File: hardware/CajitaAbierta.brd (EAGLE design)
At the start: 32.1 x 61.8 mm, 30 parts

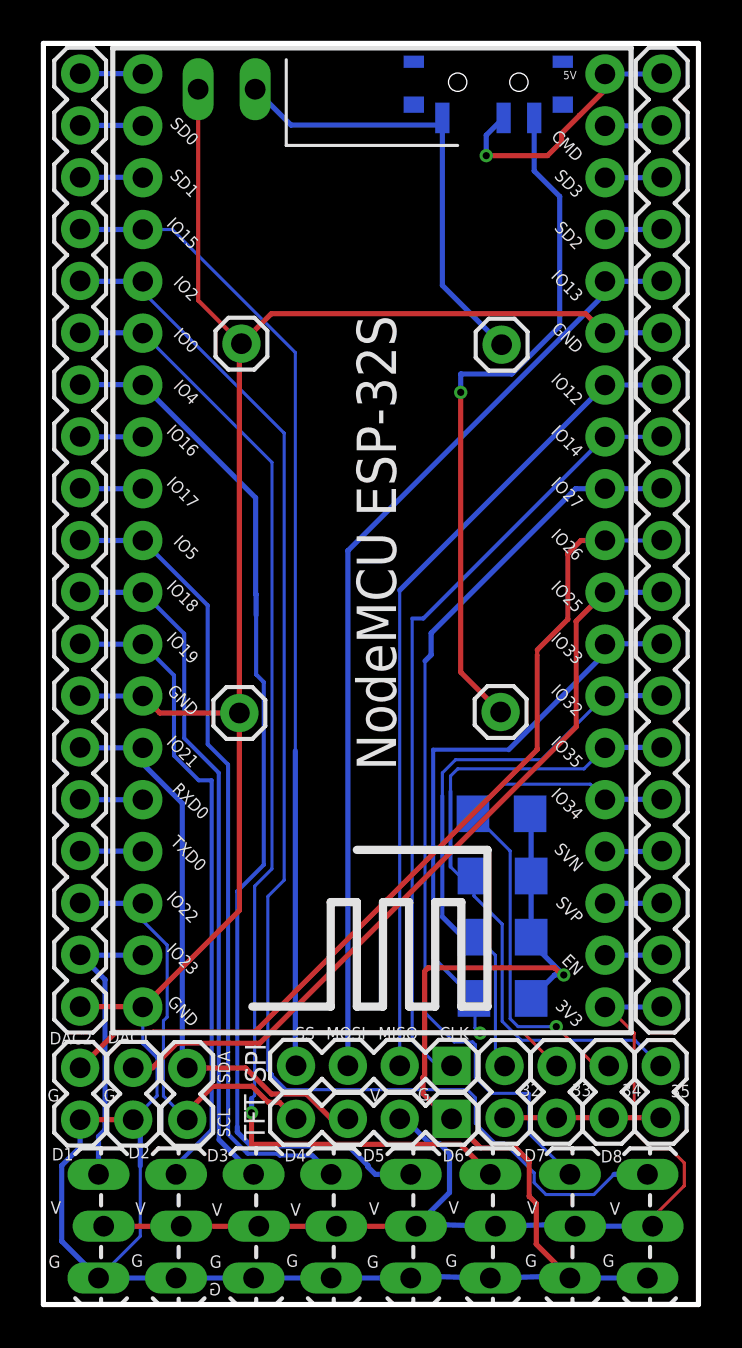
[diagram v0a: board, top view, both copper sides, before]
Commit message: v04 - changes to the TFT connections
nouvelles étiquettes (labels)
cambié sdl and sda
switch on the other side
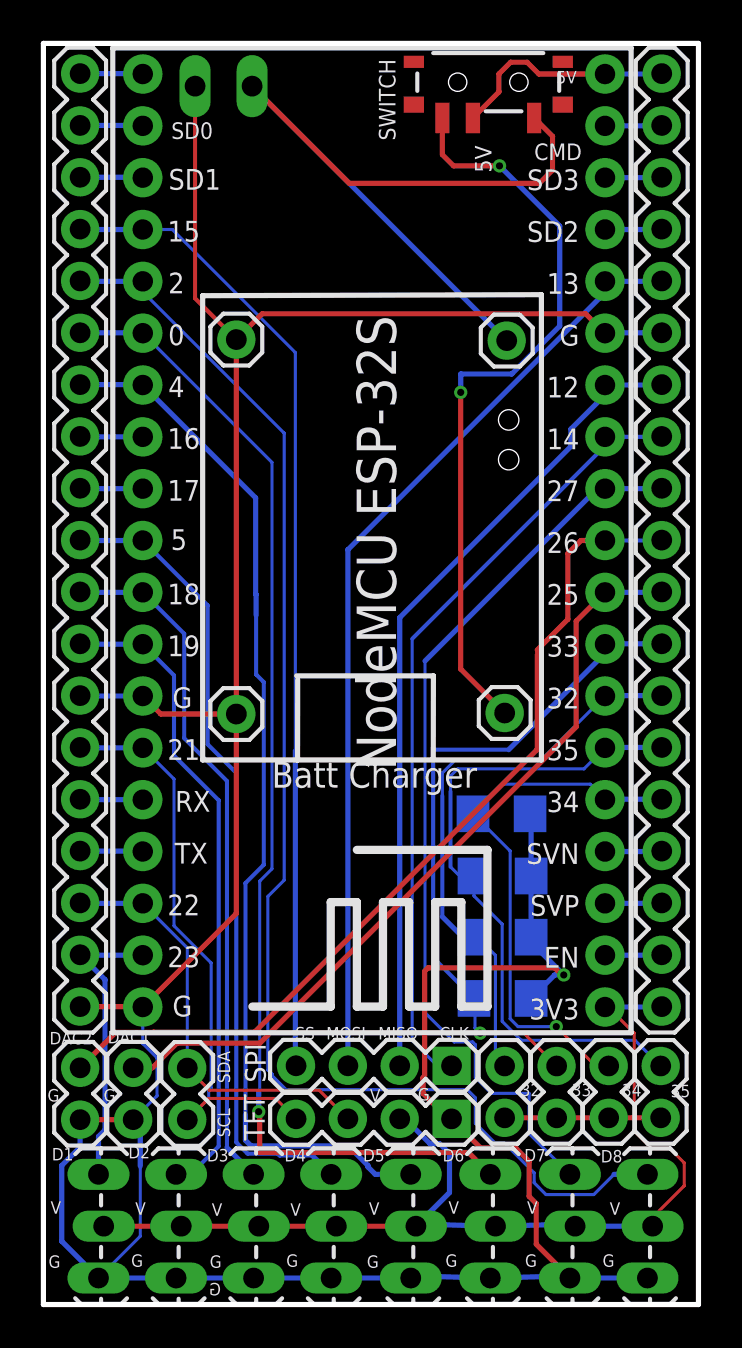
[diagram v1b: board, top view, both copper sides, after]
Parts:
- moved GND 0.32 mm to (9.45, 47.3)
- moved BATT+ 0.32 mm to (22.7, 47.2)
- moved BATT 0.21 mm to (7.56, 59.7)
- moved 5V_IN 0.21 mm to (22.6, 29.0)
- moved BAT- 0.16 mm to (9.45, 28.9)
- flipped SWITCH to the top
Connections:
- net I2C_SCL: now also I2C.2, TFT.3; no longer I2C.1, TFT.4
- net I2C_SDA: now also I2C.1, TFT.4; no longer I2C.2, TFT.3
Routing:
- net BATT+: track 22.6 -> 37.5 mm
- net 5V_IN: track 33.9 -> 37.2 mm, vias 1 -> 2
- net 5V: track 13.2 -> 11.1 mm, vias 1 -> 0
- net I2C_SDA: track 28.6 -> 29.4 mm
- net I2C_SCL: track 21.7 -> 21.0 mm
- net D7: track 45.5 -> 44.8 mm
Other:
- board text added: "UQAM UNTREF"
- board text added: "V 0.4"
- board text removed: "UQAM EAVM"
- board text removed: "V 0.3"

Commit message: Now with screw terminals
More code examples
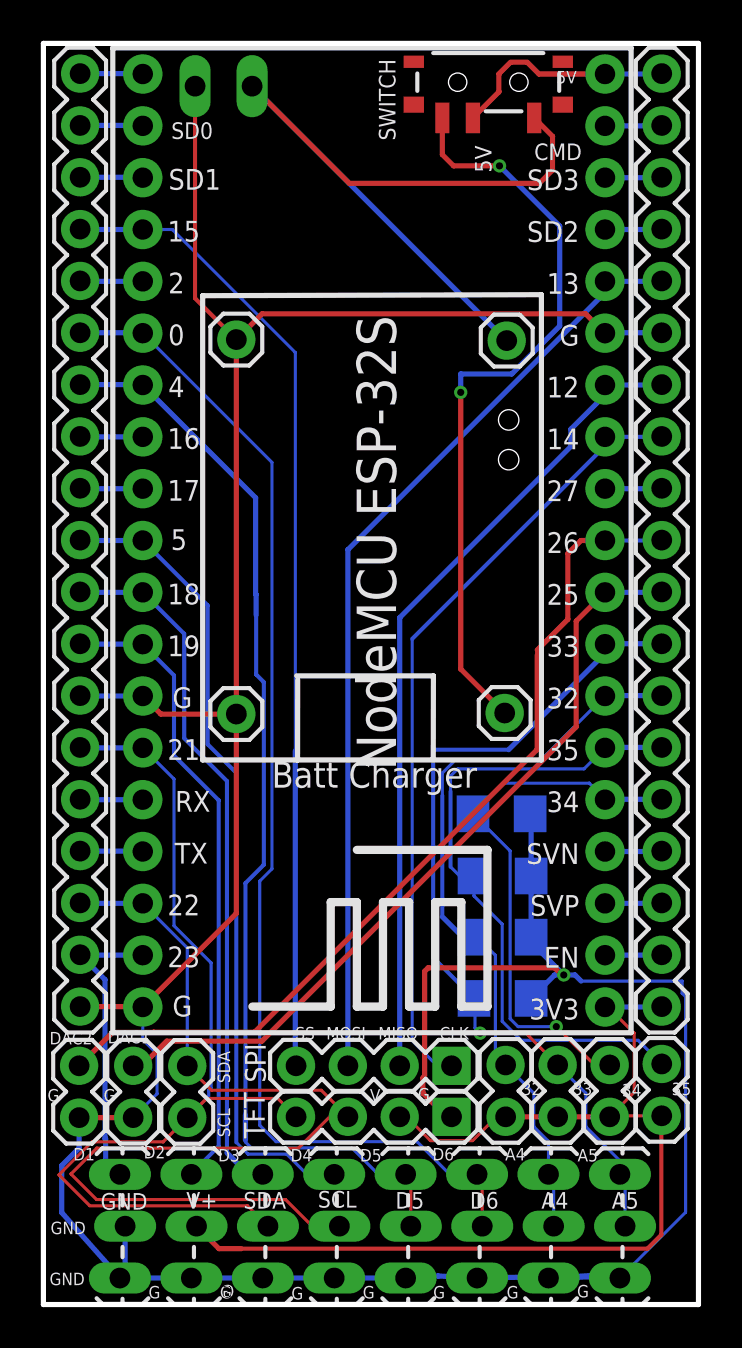
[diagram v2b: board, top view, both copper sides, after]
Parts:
- removed D7, D8: (no value), SparkFun-Connectors:1X03_LOCK_LONGPADS
- added A4, A5: (no value), SparkFun-Connectors:1X03_LOCK_LONGPADS
- moved D1 1.05 mm to (3.75, 1.30)
- moved D2 0.75 mm to (7.25, 1.30)
- moved D6 0.65 mm to (21.2, 1.30)
- moved D3 0.45 mm to (10.8, 1.30)
- moved D5 0.25 mm to (17.8, 1.30)
- moved D4 0.15 mm to (14.2, 1.30)
- moved 35 0.11 mm to (30.3, 9.25)
- moved DAC2 0.11 mm to (1.75, 11.7)
- moved DAC1 0.10 mm to (4.40, 11.7)
- moved I2C 0.10 mm to (7.05, 9.15)
- moved TFT 0.10 mm to (20.0, 9.20)
- moved 33 0.07 mm to (25.2, 9.20)
- moved 34 0.07 mm to (27.8, 9.20)
- moved 32 0.07 mm to (22.6, 9.20)
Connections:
- net 3V3: no longer D1.2, D3.2, D4.2, D5.2, D6.2, D7.2, D8.2
- net ADC4: now also A4.2, A4.3
- net ADC5: now also A5.2, A5.3
- net D5: now also D5.2
- net D6: now also D6.2
- net D7: no longer D7.3
- net D8: no longer D8.3
- net GND: now also A4.1, A5.1, D1.2; no longer D7.1, D8.1
- net I2C_SCL: now also D4.2
- net I2C_SDA: now also D3.2
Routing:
- net D8: track 67.5 -> 3.08 mm
- net D7: track 44.8 -> 2.79 mm
- net I2C_SCL: track 21.0 -> 49.8 mm
- net I2C_SDA: track 29.4 -> 47.9 mm
- net ADC5: track 32.9 -> 42.2 mm
- net ADC4: track 28.7 -> 37.5 mm
- net GND: track 171.1 -> 178.0 mm
- net 3V3: track 58.5 -> 52.5 mm
- net D5: track 51.8 -> 54.2 mm
- net D6: track 57.9 -> 59.1 mm, vias 1 -> 0
- net D2: track 31.9 -> 31.2 mm
- net D3: track 33.8 -> 34.4 mm
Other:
- board text added: "A4"
- board text added: "A5"
- board text added: "V 0.5"
- board text removed: "D8"
- board text removed: "V 0.4"
